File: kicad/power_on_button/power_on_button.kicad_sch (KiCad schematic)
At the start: 3 parts, among them J1 Conn_01x02_Pin, SW1 B3W-1000

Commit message: add powert button to menu
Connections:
- net 3.3V: now also J1.2 (Pin_2); no longer J1.1 (Pin_1)
- net Btn1: now also J1.1 (Pin_1); no longer J1.2 (Pin_2)
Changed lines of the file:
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@@
 		)
 	)
-	(label "3.3V"
+	(label "Btn1"
 		(at 44.45 96.52 0)
 		(effects
@@
 		)
 	)
-	(label "Btn1"
+	(label "3.3V"
 		(at 44.45 99.06 0)
 		(effects

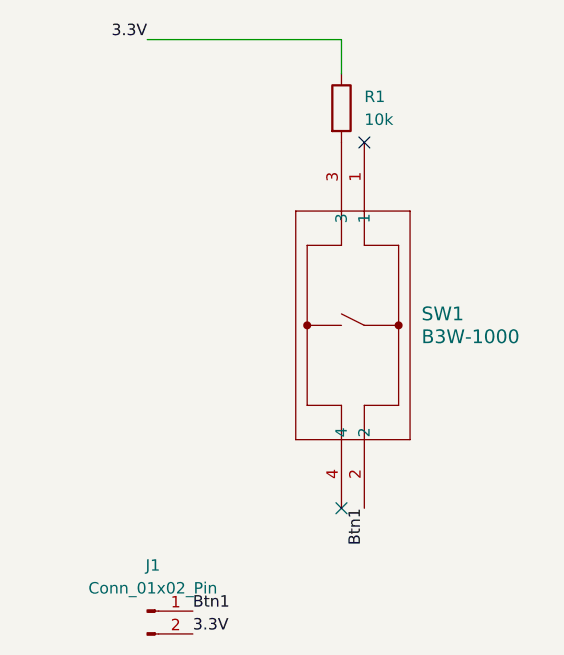
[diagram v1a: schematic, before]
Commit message: fix bug in power on button routing in hat
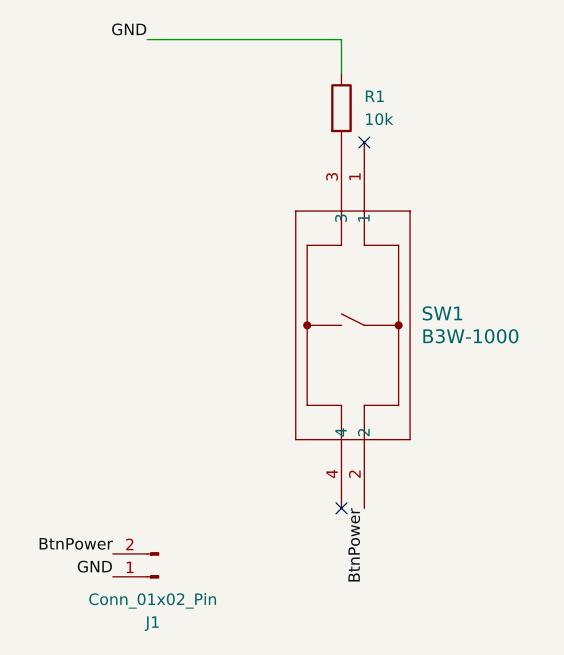
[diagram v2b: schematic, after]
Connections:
- net 3.3V renamed BtnPower
- net BtnPower: now also SW1.2; no longer R1.1
- net Btn1 renamed GND
- net GND: now also R1.1; no longer SW1.2
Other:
- moved on the sheet: J1
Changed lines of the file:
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@@
 		)
 	)
-	(label "Btn1"
+	(label "BtnPower"
 		(at 63.5 85.09 270)
 		(effects
@@
 		)
 	)
-	(label "3.3V"
+	(label "GND"
 		(at 39.37 33.02 180)
 		(effects
@@
 		)
 	)
-	(label "Btn1"
-		(at 44.45 96.52 0)
+	(label "BtnPower"
+		(at 35.56 90.17 180)
 		(effects
 			(font
 				(size 1.27 1.27)
 			)
-			(justify left bottom)
+			(justify right bottom)
 		)
 	)
-	(label "3.3V"
-		(at 44.45 99.06 0)
+	(label "GND"
+		(at 35.56 92.71 180)
 		(effects
 			(font
 				(size 1.27 1.27)
 			)
-			(justify left bottom)
+			(justify right bottom)
 		)
 	)
@@
 	(symbol
 		(lib_id "Connector:Conn_01x02_Pin")
-		(at 39.37 96.52 0)
+		(at 40.64 92.71 180)
 		(unit 1)
 		(body_style 1)
@@
 		(fields_autoplaced yes)
 		(property "Reference" "J1"
-			(at 40.005 91.44 0)
+			(at 40.005 97.79 0)
 			(show_name no)
 			(do_not_autoplace no)
@@
 		)
 		(property "Value" "Conn_01x02_Pin"
-			(at 40.005 93.98 0)
+			(at 40.005 95.25 0)
 			(show_name no)
 			(do_not_autoplace no)
@@
 		)
 		(property "Footprint" "Connector_JST:JST_XH_S2B-XH-A_1x02_P2.50mm_Horizontal"
-			(at 39.37 96.52 0)
+			(at 40.64 92.71 0)
 			(hide yes)
 			(show_name no)
@@
 		)
 		(property "Datasheet" ""
-			(at 39.37 96.52 0)
+			(at 40.64 92.71 0)
 			(hide yes)
 			(show_name no)
@@
 		)
 		(property "Description" "Generic connector, single row, 01x02, script generated"
-			(at 39.37 96.52 0)
+			(at 40.64 92.71 0)
 			(hide yes)
 			(show_name no)
